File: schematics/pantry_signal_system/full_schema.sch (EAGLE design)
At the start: 79 parts, among them J1 JST-XH254-2P, J2 JST-XH254-3P, J3 JST-XH254-2P, J4 JST-XH254-3P, J5 JST-XH254-2P, J6 JST-XH254-2P, J7 JST-XH254-2P, J8 JST-XH254-2P, Q1 STP14NM50N, Q12 STP14NM50N, Q13 STP14NM50N, Q14 2N3904, Q2 STP14NM50N, Q7 2N3904, Q8 2N3904, Q9 STP14NM50N, SW1 SWITCH, SW2 SWITCH, U1 MCP1703T-5002E/CB, U10 FAN73611, U11 FAN73611, U2 AD8544, U3 ATTINY13, U4 ATMEGA328P, U5 MCP1703T-5002E/CB, U6 2004A I2C, U7 BME280BME280-CONNECTOR-ONLY, U8 E220-900T22D, U9 FAN73611

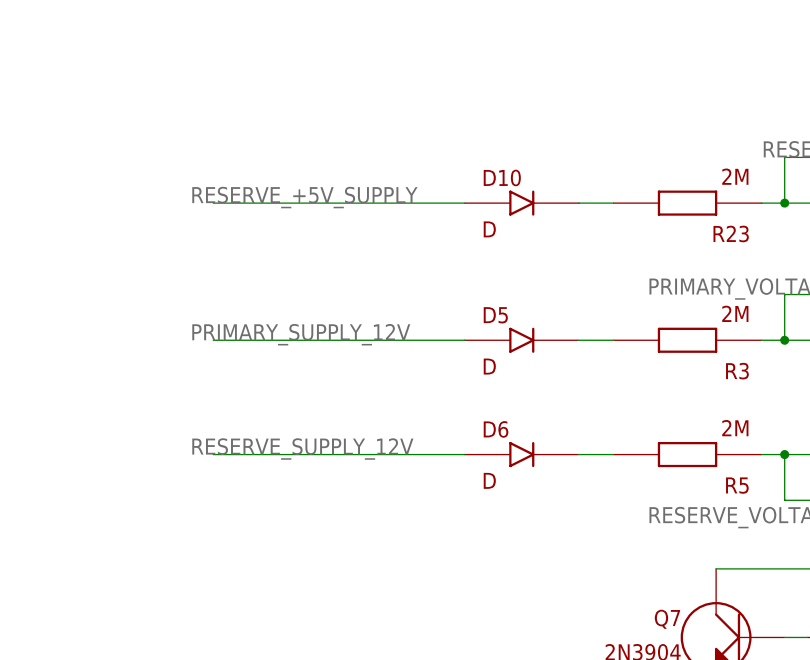
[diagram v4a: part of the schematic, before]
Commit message: Start working under supply schema
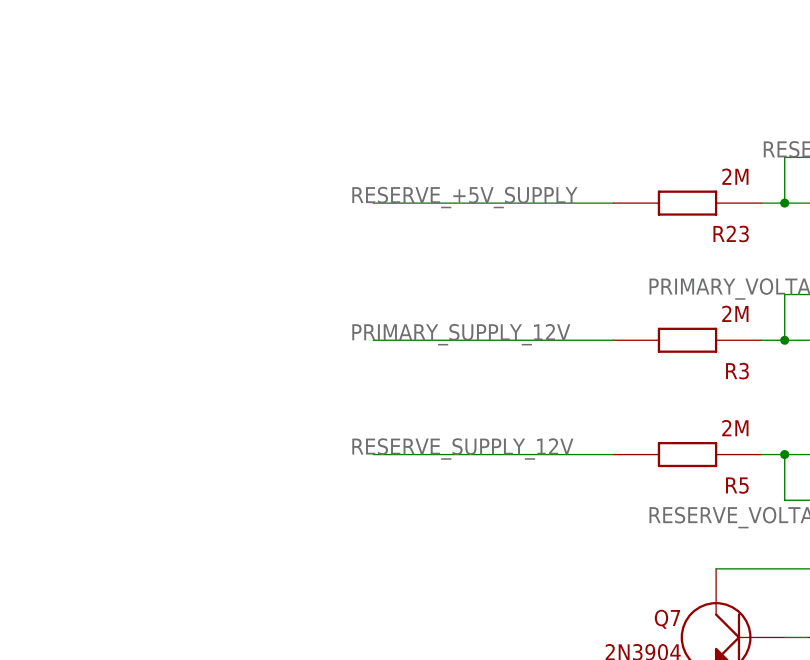
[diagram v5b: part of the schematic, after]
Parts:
- removed D10, D5, D6: D, my_devices:D
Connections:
- removed net N$2: D5.P$2, R3.P$2
- removed net N$29: D10.P$2, R23.P$2
- removed net N$5: D6.P$2, R5.P$2
- net PRIMARY_SUPPLY_12V: now also R3.P$2; no longer D5.P$1
- net RESERVE_+5V_SUPPLY: now also R23.P$2; no longer D10.P$1
- net RESERVE_SUPPLY_12V: now also R5.P$2; no longer D6.P$1
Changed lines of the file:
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@@
 <part name="R6" library="my_devices" deviceset="R" device="" value="1M"/>
 <part name="GND16" library="supply1" library_urn="urn:adsk.eagle:library:371" deviceset="GND" device=""/>
-<part name="D5" library="my_devices" deviceset="D" device=""/>
-<part name="D6" library="my_devices" deviceset="D" device=""/>
 <part name="Q7" library="my_devices" deviceset="TRANSISTOR_NPN" device="" value="2N3904"/>
 <part name="J4" library="my_devices" deviceset="JST-XH254-3P" device=""/>
@@
 <part name="R23" library="my_devices" deviceset="R" device="" value="2M"/>
 <part name="R24" library="my_devices" deviceset="R" device="" value="1M"/>
-<part name="D10" library="my_devices" deviceset="D" device=""/>
 <part name="U9" library="my_devices" deviceset="FAN73611" device=""/>
 <part name="GND7" library="supply1" library_urn="urn:adsk.eagle:library:371" deviceset="GND" device=""/>
@@
 <attribute name="VALUE" x="360.68" y="71.12" size="1.778" layer="96"/>
 </instance>
-<instance part="D5" gate="G$1" x="307.34" y="76.2" smashed="yes" grouprefs="SUPPLY_AVR">
-<attribute name="NAME" x="301.625" y="78.105" size="1.778" layer="94"/>
-<attribute name="VALUE" x="301.625" y="72.39" size="1.778" layer="94"/>
-</instance>
-<instance part="D6" gate="G$1" x="307.34" y="63.5" smashed="yes" grouprefs="SUPPLY_AVR">
-<attribute name="NAME" x="301.625" y="65.405" size="1.778" layer="94"/>
-<attribute name="VALUE" x="301.625" y="59.69" size="1.778" layer="94"/>
-</instance>
 <instance part="Q7" gate="G$1" x="327.66" y="43.18" smashed="yes" rot="MR0" grouprefs="SUPPLY_AVR">
 <attribute name="NAME" x="323.85" y="44.45" size="1.778" layer="94" rot="MR0"/>
@@
 <attribute name="NAME" x="354.33" y="88.9" size="1.778" layer="94" rot="R180"/>
 <attribute name="VALUE" x="354.33" y="95.25" size="1.778" layer="94" rot="R180"/>
-</instance>
-<instance part="D10" gate="G$1" x="307.34" y="91.44" smashed="yes" grouprefs="SUPPLY_AVR">
-<attribute name="NAME" x="301.625" y="93.345" size="1.778" layer="94"/>
-<attribute name="VALUE" x="301.625" y="87.63" size="1.778" layer="94"/>
 </instance>
 <instance part="U9" gate="G$1" x="-12.7" y="-91.44" smashed="yes" grouprefs="DISCHARGE_CONTROL_AND_POWER_SWITCH">
@@
 </segment>
 <segment>
-<pinref part="D6" gate="G$1" pin="P$1"/>
-<wire x1="299.72" y1="63.5" x2="271.78" y2="63.5" width="0.1524" layer="91" grouprefs="SUPPLY_AVR"/>
-<label x="269.24" y="63.5" size="1.778" layer="95" grouprefs="SUPPLY_AVR"/>
+<wire x1="316.23" y1="63.5" x2="289.56" y2="63.5" width="0.1524" layer="91" grouprefs="SUPPLY_AVR"/>
+<label x="287.02" y="63.5" size="1.778" layer="95" grouprefs="SUPPLY_AVR"/>
+<pinref part="R5" gate="G$1" pin="P$2"/>
 </segment>
 <segment>
@@
 </segment>
 <segment>
-<pinref part="D5" gate="G$1" pin="P$1"/>
-<wire x1="299.72" y1="76.2" x2="271.78" y2="76.2" width="0.1524" layer="91" grouprefs="SUPPLY_AVR"/>
-<label x="269.24" y="76.2" size="1.778" layer="95" grouprefs="SUPPLY_AVR"/>
+<wire x1="316.23" y1="76.2" x2="289.56" y2="76.2" width="0.1524" layer="91" grouprefs="SUPPLY_AVR"/>
+<label x="287.02" y="76.2" size="1.778" layer="95" grouprefs="SUPPLY_AVR"/>
+<pinref part="R3" gate="G$1" pin="P$2"/>
 </segment>
 <segment>
@@
 <wire x1="287.655" y1="33.02" x2="264.16" y2="33.02" width="0.1524" layer="91" grouprefs="SUPPLY_AVR"/>
 <label x="256.54" y="33.02" size="1.778" layer="95" grouprefs="SUPPLY_AVR"/>
-</segment>
-</net>
-<net name="N$2" class="0">
-<segment>
-<pinref part="D5" gate="G$1" pin="P$2"/>
-<pinref part="R3" gate="G$1" pin="P$2"/>
-<wire x1="312.42" y1="76.2" x2="316.23" y2="76.2" width="0.1524" layer="91" grouprefs="SUPPLY_AVR"/>
-</segment>
-</net>
-<net name="N$5" class="0">
-<segment>
-<pinref part="D6" gate="G$1" pin="P$2"/>
-<pinref part="R5" gate="G$1" pin="P$2"/>
-<wire x1="312.42" y1="63.5" x2="316.23" y2="63.5" width="0.1524" layer="91" grouprefs="SUPPLY_AVR"/>
 </segment>
 </net>
@@
 </segment>
 <segment>
-<pinref part="D10" gate="G$1" pin="P$1"/>
-<wire x1="299.72" y1="91.44" x2="271.78" y2="91.44" width="0.1524" layer="91" grouprefs="SUPPLY_AVR"/>
-<label x="269.24" y="91.44" size="1.778" layer="95" grouprefs="SUPPLY_AVR"/>
+<wire x1="316.23" y1="91.44" x2="289.56" y2="91.44" width="0.1524" layer="91" grouprefs="SUPPLY_AVR"/>
+<label x="287.02" y="91.44" size="1.778" layer="95" grouprefs="SUPPLY_AVR"/>
+<pinref part="R23" gate="G$1" pin="P$2"/>
 </segment>
 </net>
@@
 </segment>
 </net>
-<net name="N$29" class="0">
-<segment>
-<pinref part="D10" gate="G$1" pin="P$2"/>
-<pinref part="R23" gate="G$1" pin="P$2"/>
-<wire x1="312.42" y1="91.44" x2="316.23" y2="91.44" width="0.1524" layer="91" grouprefs="SUPPLY_AVR"/>
-</segment>
-</net>

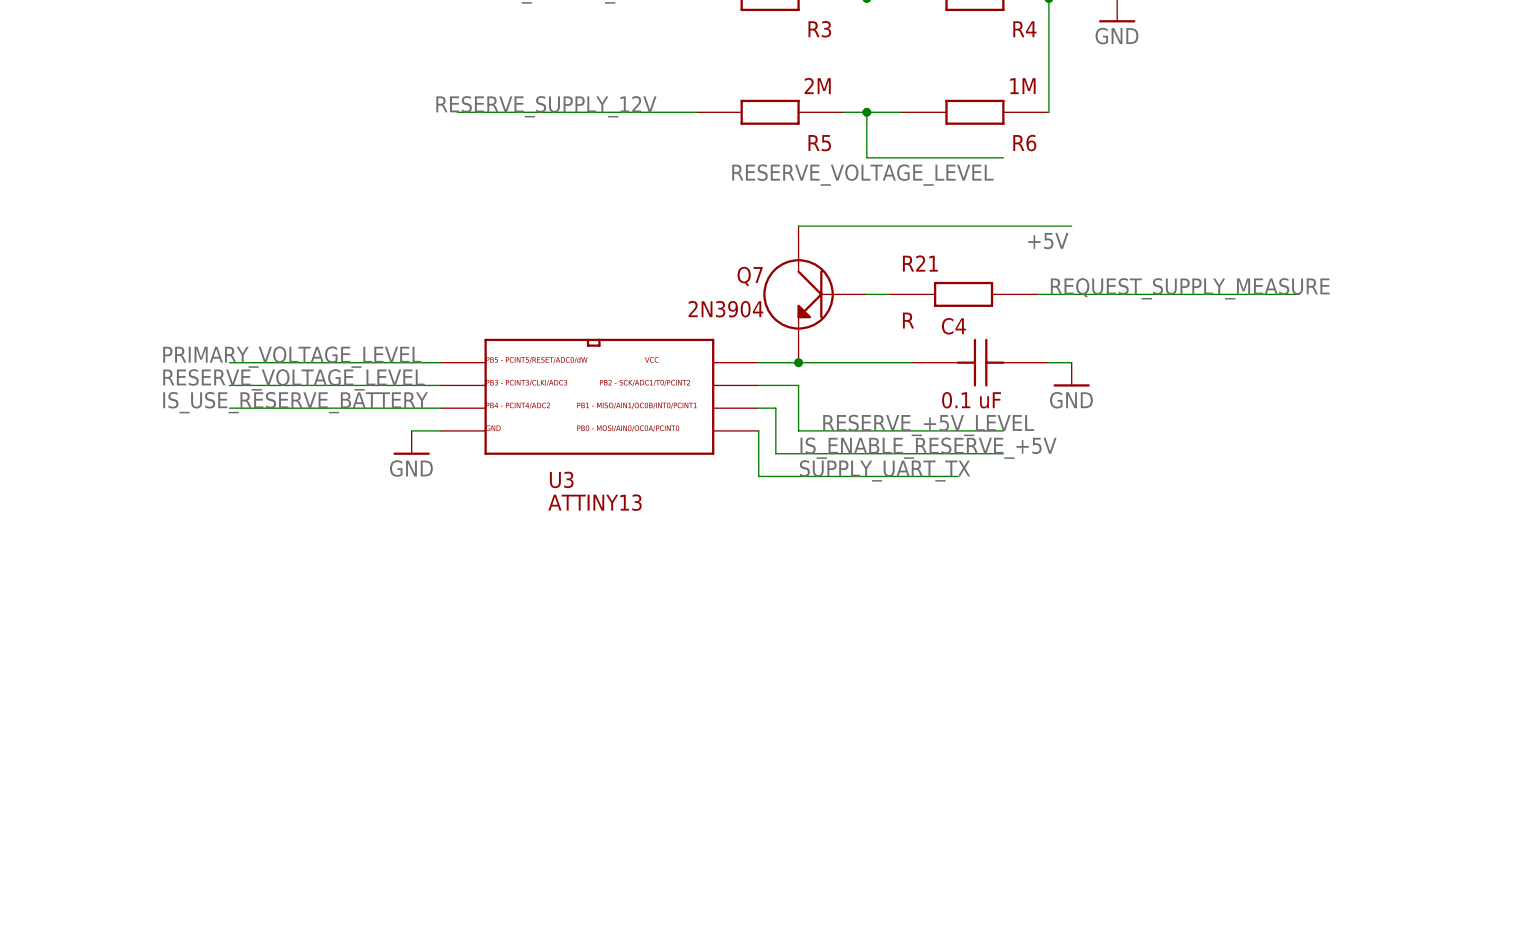
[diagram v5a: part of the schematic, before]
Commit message: Added programmer connector for ATTiny
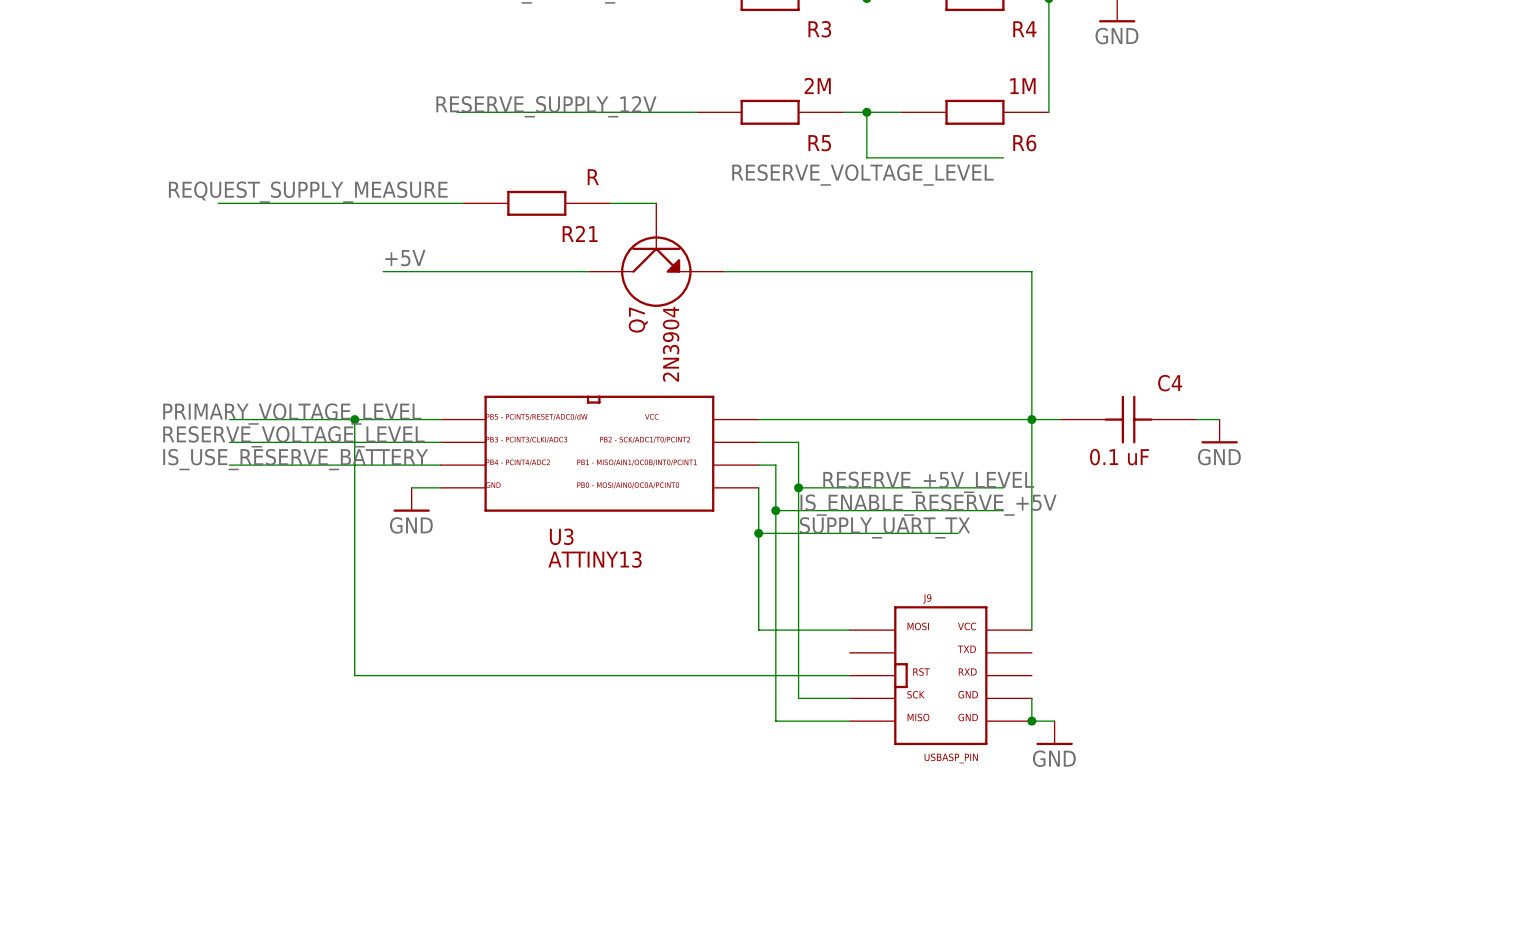
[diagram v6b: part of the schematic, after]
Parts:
- added J9: USBASP_PIN, my_devices:USBASP_PIN
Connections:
- removed net N$9: C4.P$1, Q7.E, U3.VCC
- new net N$2: C4.P$1, J9.VCC, Q7.E, U3.VCC
- net GND: now also J9.GND, J9.GND1
- net IS_ENABLE_RESERVE_+5V: now also J9.MISO
- net PRIMARY_VOLTAGE_LEVEL: now also J9.RESET
- net RESERVE_+5V_LEVEL: now also J9.SCK
- net SUPPLY_UART_TX: now also J9.MOSI
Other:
- moved on the sheet: C4, Q7, R21, U3

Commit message: Working under supplu control
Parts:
- added D5: D, my_devices:D
- added R10, R11: 2M, my_devices:R
- C5: value C-1 -> 0.1 uF
- D1, D2, D7: value D -> BAT41
- D3, D4, D8, D9: value D -> BAT760
- R22: value 620 -> 1K
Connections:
- new net N$9: D5.P$2, U2.D+
- net IS_PRIMARY_BATTERY_OK: now also R10.P$2
- net IS_RESERVE_BATTERY_OK: now also D5.P$1, R11.P$1; no longer U2.D+
- net N$3: now also R10.P$1
- net N$8: now also R11.P$2

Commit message: Continue working under supply control schematics. Changed N-channel mosfets to P-channel mosfets. Small changes in logic control module
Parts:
- removed Q2: STP14NM50N, my_devices:MOSFET_N
- added U12: NC7WZ04, my_devices:INVERTER._X2
- D1, D2, D7: value BAT41 -> MBR130LSFT1G
- D3, D4, D8, D9: value BAT760 -> MBR130LSFT1G
- Q1: value STP14NM50N -> FDS4935A; device my_devices:MOSFET_N -> my_devices:MOSFET_P_X2
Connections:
- new net N$18: U12.Y1, U9.IN
- new net N$19: U10.IN, U12.Y2
- net +12V: now also J3.PIN1; no longer Q9.D
- net GND: now also Q9.S, U12.GND; no longer J3.PIN2
- net IS_PRIMARY_BATTERY_OK: now also U12.A1; no longer U9.IN
- net IS_USE_RESERVE_BATTERY: now also U12.A2; no longer U10.IN
- net N$12: now also Q1.D21, Q1.D22; no longer Q1.S
- net N$13: now also Q1.D11, Q1.D12; no longer Q2.S
- net N$4: now also J3.PIN2, Q9.D; no longer J3.PIN1, Q9.S
- net PRIMARY_SUPPLY_12V: now also Q1.S2; no longer Q1.D, U10.VB, U10.VDD
- net RESERVE_SUPPLY_12V: now also Q1.S1, U10.VB, U10.VDD; no longer Q2.D
- net SUPPLY_CONTROL_+5V: now also U12.VCC
- net USE_PRIMARY_BATTERY: now also Q1.G2; no longer Q1.G
- net USE_RESERVE_BATTERY: now also Q1.G1; no longer Q2.G
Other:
- moved on the sheet: C2, C3, D3, D4, D5, D8, D9, FAN1, J3, J5, Q14, Q9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
